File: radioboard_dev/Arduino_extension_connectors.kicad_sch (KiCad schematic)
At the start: 13 parts

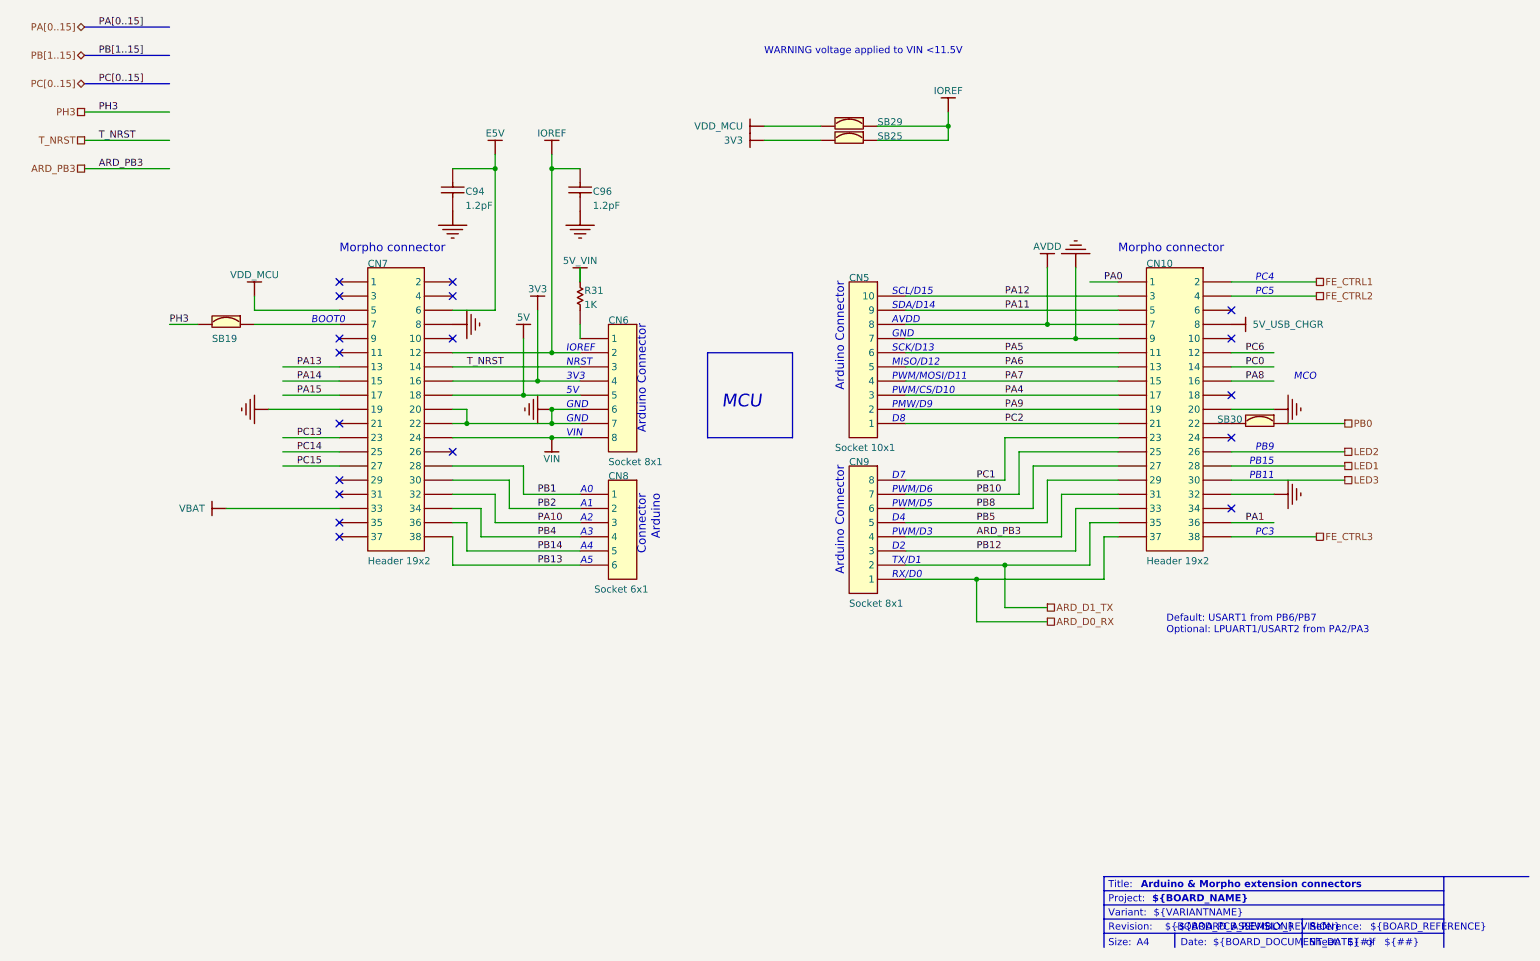
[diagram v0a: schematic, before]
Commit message: added components
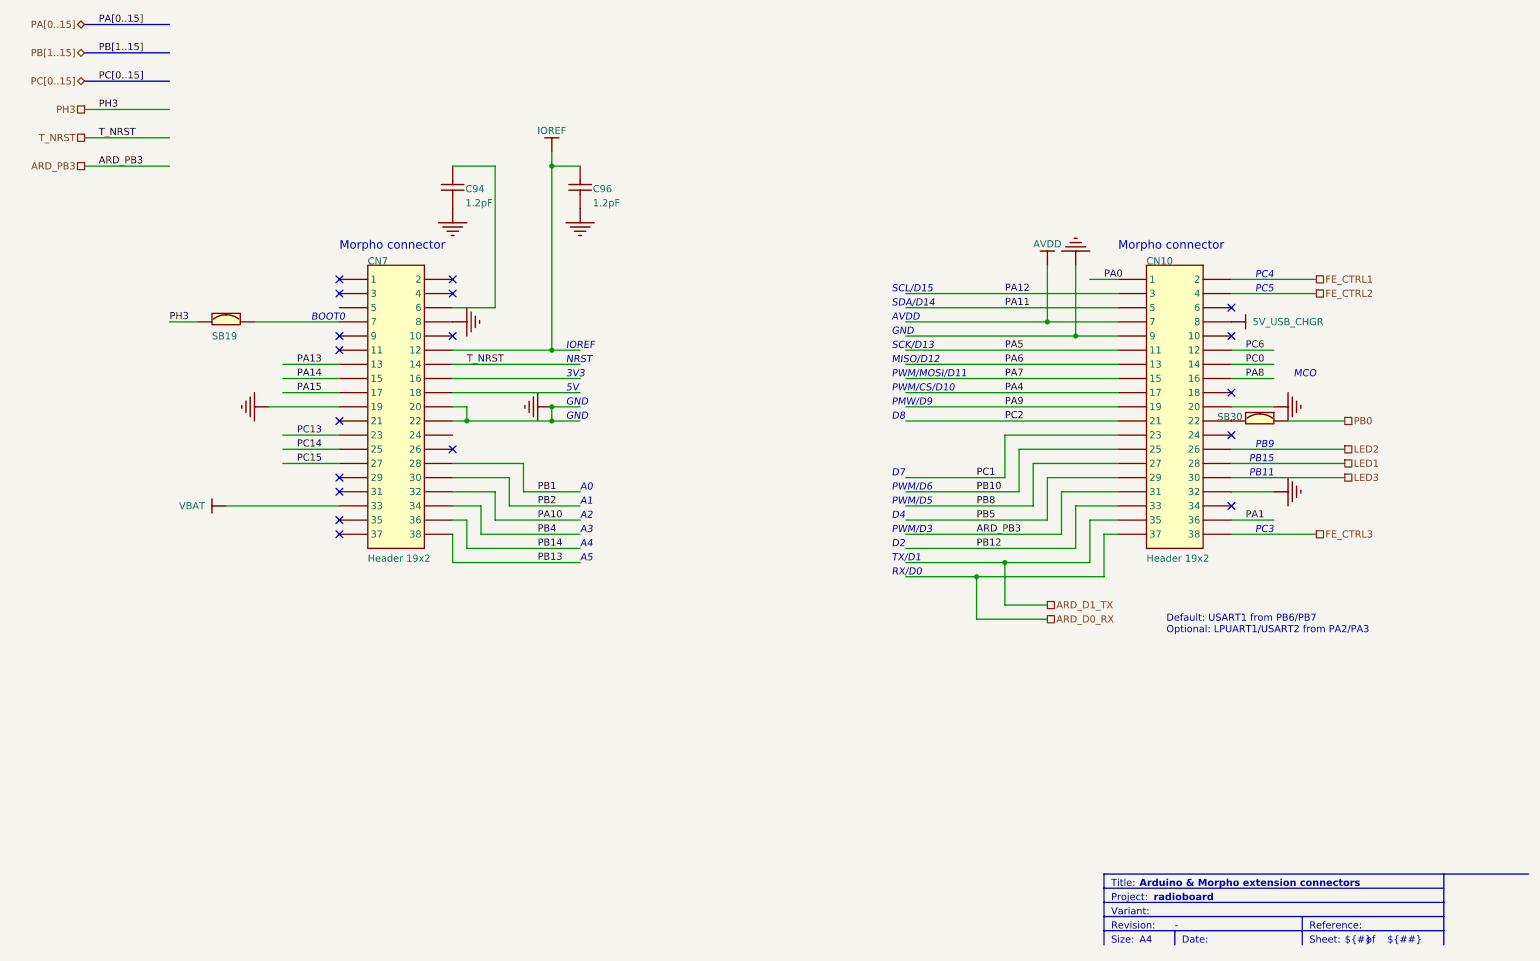
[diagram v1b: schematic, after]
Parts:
- removed CN5: (no value), CON_SAMTEC_SSW-110-03-X-S, symbol MB1389-altium-import:U_Arduino_extension_connectors_0_Socket 10x1
- removed CN6: (no value), CON_SAMTEC_SSW-108-03-X-S, symbol MB1389-altium-import:U_Arduino_extension_connectors_2_Socket 8x1
- removed CN8: (no value), CON_SAMTEC_SSW-106-03-X-S, symbol MB1389-altium-import:U_Arduino_extension_connectors_0_Socket 6x1
- removed CN9: (no value), CON_SAMTEC_SSW-108-03-X-S, symbol MB1389-altium-import:U_Arduino_extension_connectors_0_Socket 8x1
- removed R31: (no value), R0603, symbol MB1389-altium-import:U_Arduino_extension_connectors_1_Resistor
- removed SB25, SB29: (no value), SOLDER-BRIDGE_R0603-0R, symbol MB1389-altium-import:U_Arduino_extension_connectors_0_SB_ON
- CN10, CN7, SB19, SB30: value (none) -> ~
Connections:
- net 3V3: no longer names the net of CN7.16
- net 5V: no longer names the net of CN7.18
- net E5V: no longer names the net of C94.2, CN7.6
- net VDD_MCU: no longer names the net of CN7.5
- net VIN: no longer names the net of CN7.24
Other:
- note added: "radioboard"
- note removed: "${BOARD_ASSEMBLY_REVISION}"
- note removed: "${BOARD_DOCUMENT_DATE}"
- note removed: "${BOARD_NAME}"
- note removed: "${BOARD_PCB_REVISION}"
- note removed: "${BOARD_REFERENCE}"
- note removed: "${VARIANTNAME}"
- note removed: "Arduino"
- note removed: "Arduino Connector"
- note removed: "Connector"
- note removed: "MCU"
- note removed: "VIN"
- note removed: "WARNING voltage applied to VIN <11.5V"
